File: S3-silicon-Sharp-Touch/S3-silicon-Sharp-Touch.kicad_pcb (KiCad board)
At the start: 4 copper layers, 79.8 x 44.7 mm, 64 parts, among them IC1 ESP32-S3FN8, J1 USB_C_Receptacle_USB2.0, J2 Conn_01x06_Socket, J3 Conn_01x11_Socket, J5 FH52-10S-0.5SH_99, J6 5024260810, J7 S2B-PH-SM4-TB_LF__SN_, Q1 MMBT3904, Q2 MMBT3904, Q3 Si2301CDS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

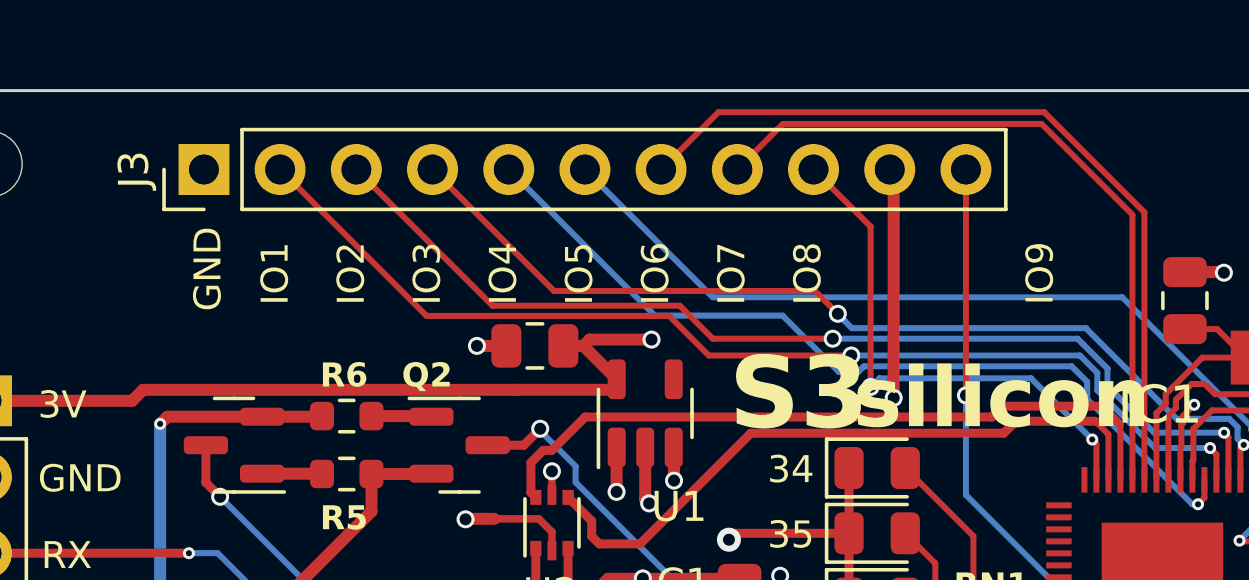
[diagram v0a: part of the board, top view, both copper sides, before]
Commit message: Update S3 silk
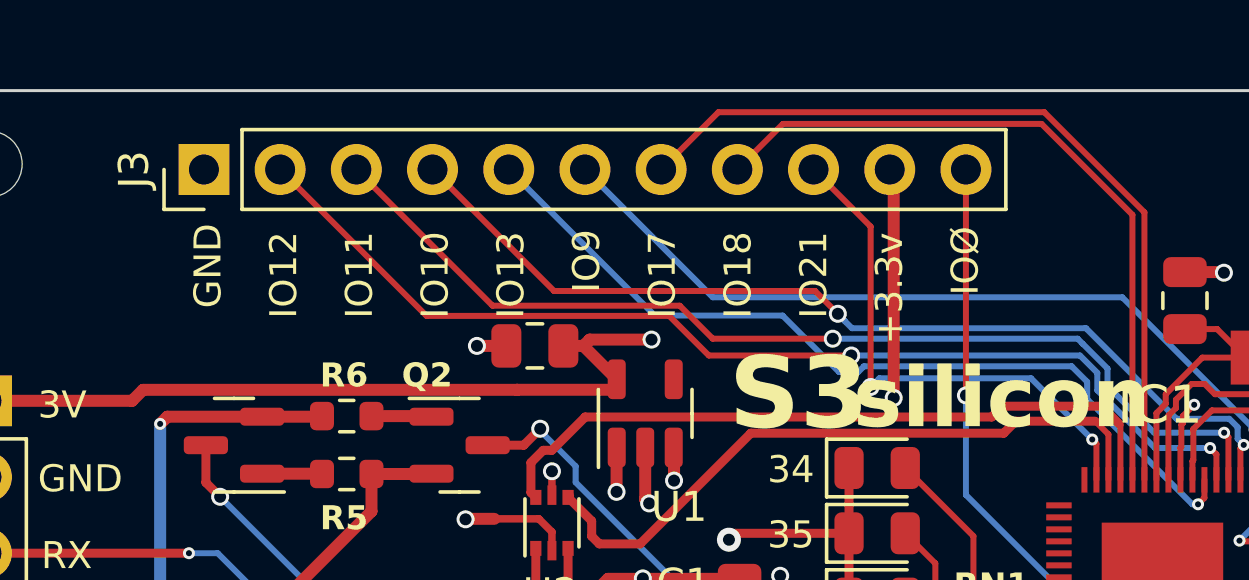
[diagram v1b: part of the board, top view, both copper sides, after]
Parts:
- added G***: LOGO, LOGO, B.Cu at (67.7, 59.6)
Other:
- board text added: "+3.3v"
- board text added: "IO10"
- board text added: "IO11"
- board text added: "IO12"
- board text added: "IO13"
- board text added: "IO17"
- board text added: "IO18"
- board text added: "IO21"
- board text added: "IOØ"
- board text added: "LCD IOs: IO - - - - - - 1 SPI_CLK 2 SPI_MOSI 3 CS 4 DISPON (pulled up) 14 EXTMODE"
- board text added: "TOUCH BITCH IO - - - - - 7 SCL (I2C) 8 SDA (I2C) 5 REST 6 IRQ (Interrupt)"
- board text removed: "IO1"
- board text removed: "IO2"
- board text removed: "IO3"
- board text removed: "IO4"
- board text removed: "IO5"
- board text removed: "IO6"
- board text removed: "IO7"
- board text removed: "IO8"

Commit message: 1.0 sent to fabrication
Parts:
- moved D7 3.80 mm to (59.7, 62.0), turned to -45 degrees
- moved D6 2.34 mm to (55.8, 61.9), turned to -135 degrees
- moved D1 0.94 mm to (59.8, 51.5), turned to 45 degrees
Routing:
- net VBUS: track 54.9 -> 60.3 mm
- net Net-(D6-K): track 2.14 -> 5.15 mm
- net Net-(D7-K): track 4.52 -> 6.96 mm
- net GND: track 58.7 -> 59.6 mm
- net VDD33: track 153.9 -> 154.5 mm
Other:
- board text added: "LCD pins: IO - - - - - - 1 SPI_CLK 2 SPI_MOSI 3 CS 4 DISPON (pulled up) 14 EXTMODE"
- board text added: "RDY"
- board text added: "TOUCH"
- board text added: "TOUCH BITCH IO - - - - - 7 SCL I2C 8 SDA I2C 5 REST 6 IRQ (Interrupt)"
- board text removed: "LCD IOs: IO - - - - - - 1 SPI_CLK 2 SPI_MOSI 3 CS 4 DISPON (pulled up) 14 EXTMODE"
- board text removed: "TOUCH BITCH IO - - - - - 7 SCL (I2C) 8 SDA (I2C) 5 REST 6 IRQ (Interrupt)"

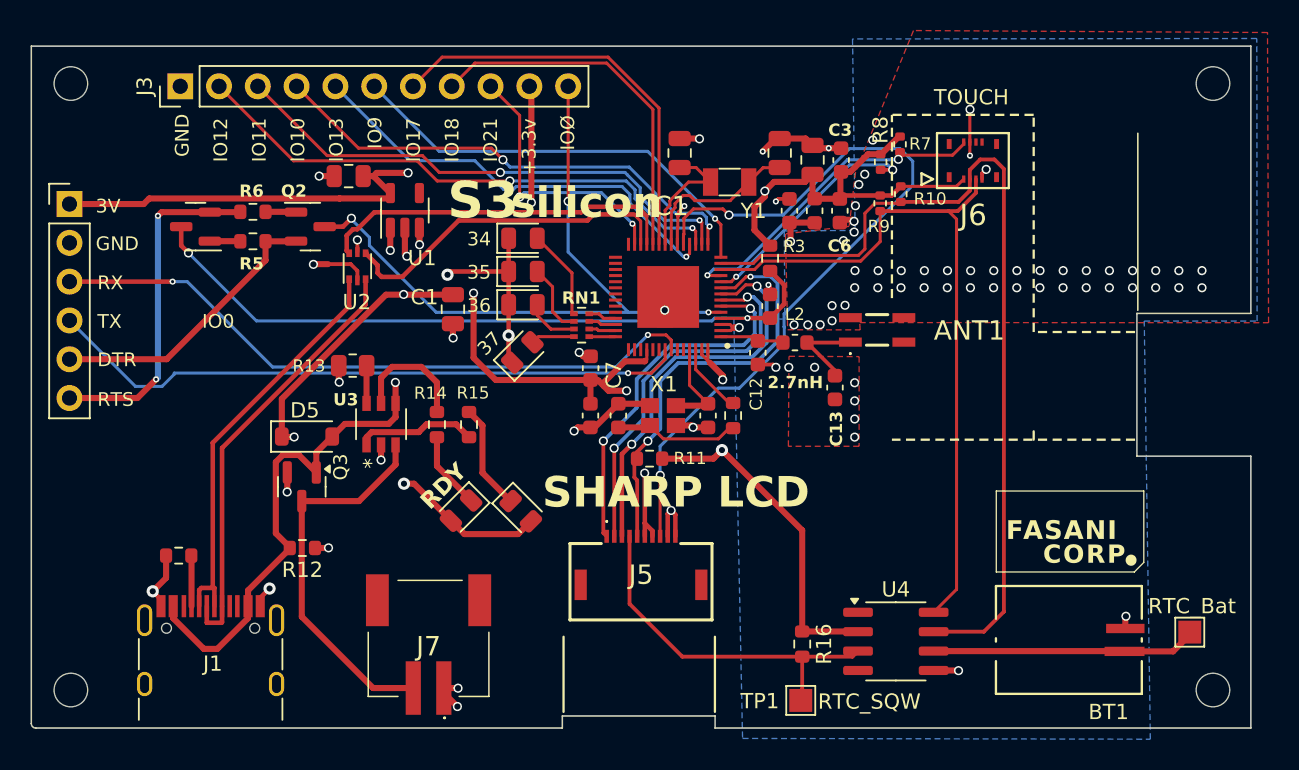
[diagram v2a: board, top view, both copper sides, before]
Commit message: Update BT1 routing because bad polarity
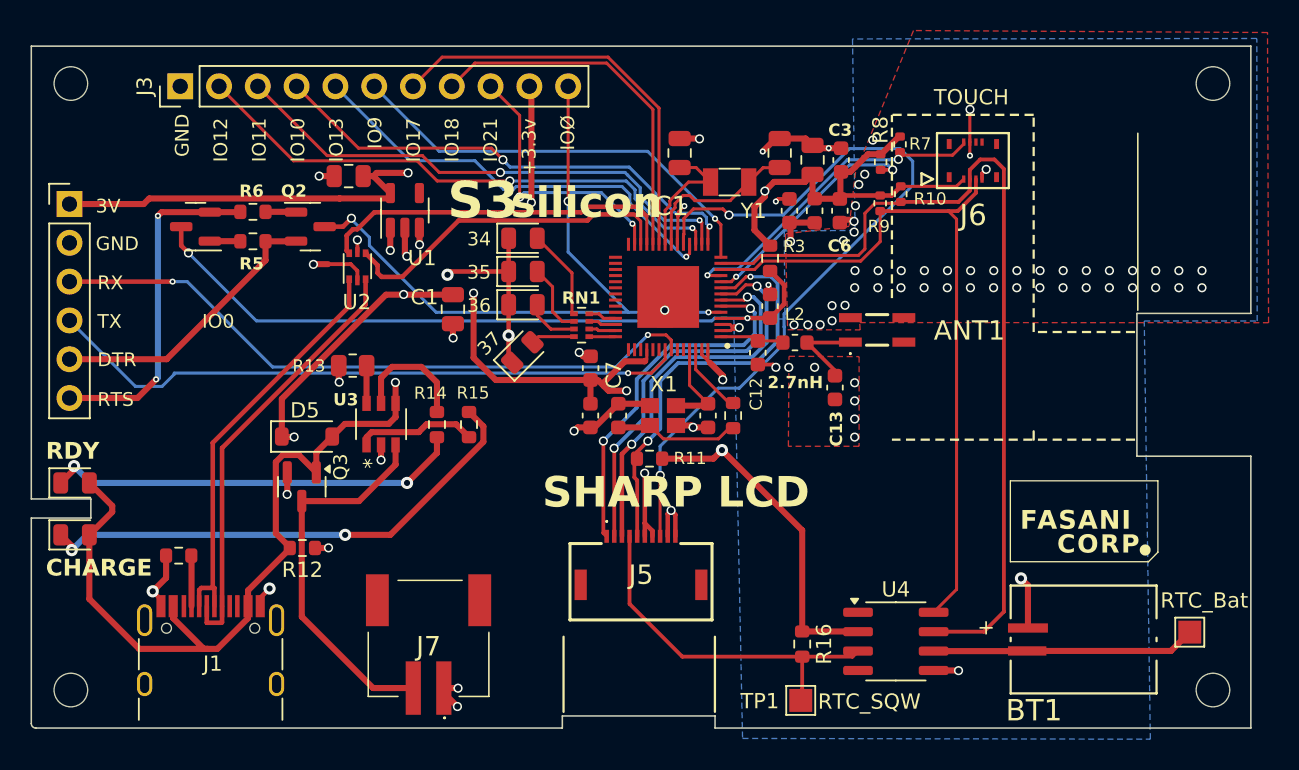
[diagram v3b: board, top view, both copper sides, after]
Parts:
- moved D7 29.2 mm to (30.5, 63.5), turned to 0 degrees
- moved D6 25.3 mm to (30.5, 60.1), turned to 0 degrees
- moved BT1 0.97 mm to (96.5, 70.3), turned to 0 degrees
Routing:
- net Net-(D7-K): track 6.96 -> 33.5 mm, vias 0 -> 2
- net Net-(D6-K): track 5.15 -> 27.5 mm, vias 0 -> 2
- net GND: track 59.6 -> 62.2 mm
- net VBUS: track 60.3 -> 61.3 mm, vias 3 -> 2
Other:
- outline, holes or cut-outs redrawn
- board text added: "CHARGE"

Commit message: Move touch 2 mm right
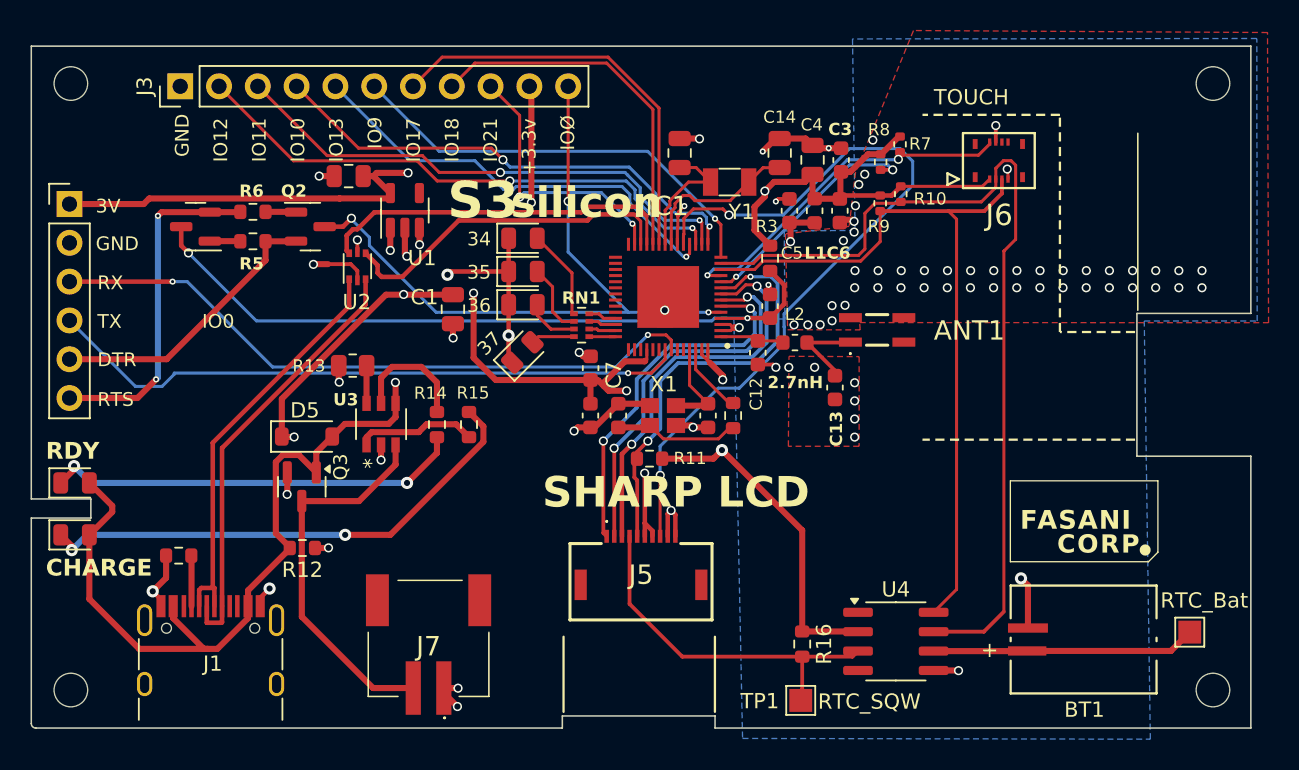
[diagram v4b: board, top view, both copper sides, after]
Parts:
- moved J6 1.70 mm to (91.0, 39.0)
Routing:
- net GND: track 62.2 -> 60.3 mm, vias 79 -> 78
- net /SCL: track 48.0 -> 49.7 mm
- net VDD33: track 154.5 -> 156.2 mm
- net /TOUCH_IRQ: track 21.8 -> 23.5 mm
- net /TOUCH_REST: track 22.2 -> 23.5 mm
- net /SDA: track 57.9 -> 59.0 mm

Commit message: Corrections heading to Rev 1.1 (Bottom ROW of Touch RIGHT!)
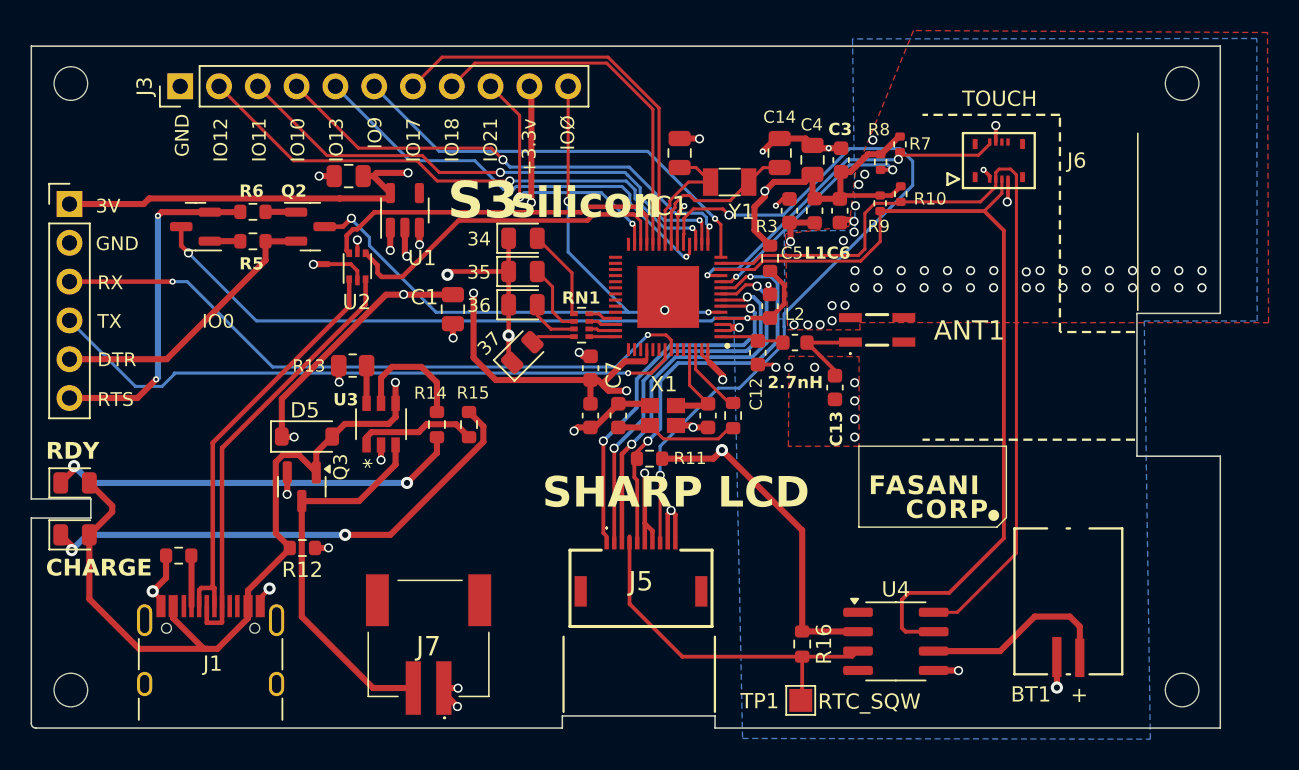
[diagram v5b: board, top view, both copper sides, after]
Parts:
- removed TP2: RTC_INT, TestPoint:TestPoint_Pad_1.5x1.5mm
- moved BT1 2.69 mm to (95.6, 67.9), turned to 90 degrees
- moved H2 2.02 mm to (103.0, 34.0)
- moved J5 0.43 mm to (67.6, 67.0)
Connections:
- IC1 pad 12: /SCL -> /SDA
- IC1 pad 13: /SDA -> /SCL
- R10 pad 2: /SDA -> /SCL
- R9 pad 2: /SCL -> /SDA
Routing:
- net VDD33: track 156.2 -> 167.8 mm, vias 8 -> 9
- net /SCL: track 49.7 -> 55.8 mm
- net VDD_RTC: track 17.3 -> 12.8 mm
- net /SDA: track 59.0 -> 56.9 mm
- net /TOUCH_REST: track 23.5 -> 22.1 mm
- net GND: track 60.3 -> 58.9 mm
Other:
- board size 79.8 x 44.7 mm -> 77.8 x 44.7 mm
- board text removed: "RTC_Bat"

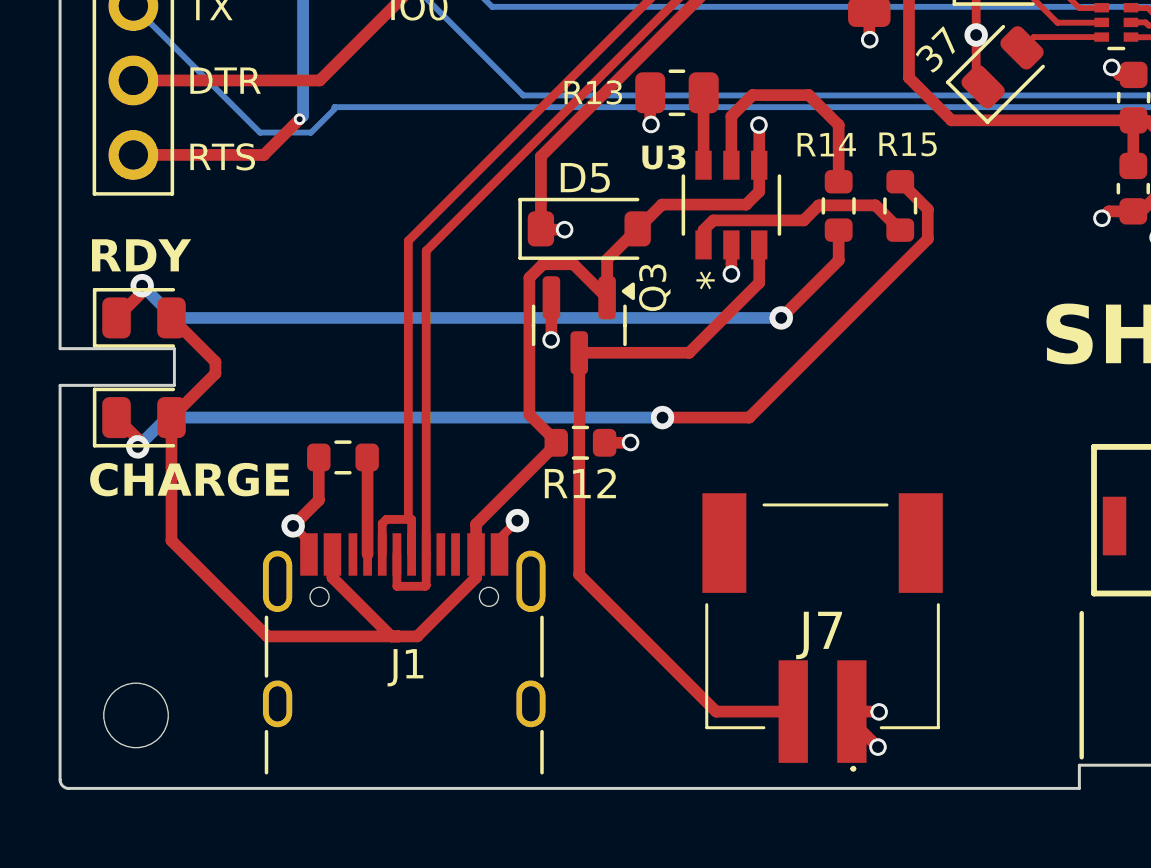
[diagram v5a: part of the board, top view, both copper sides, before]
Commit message: Update TOUCH pinout in PCBs
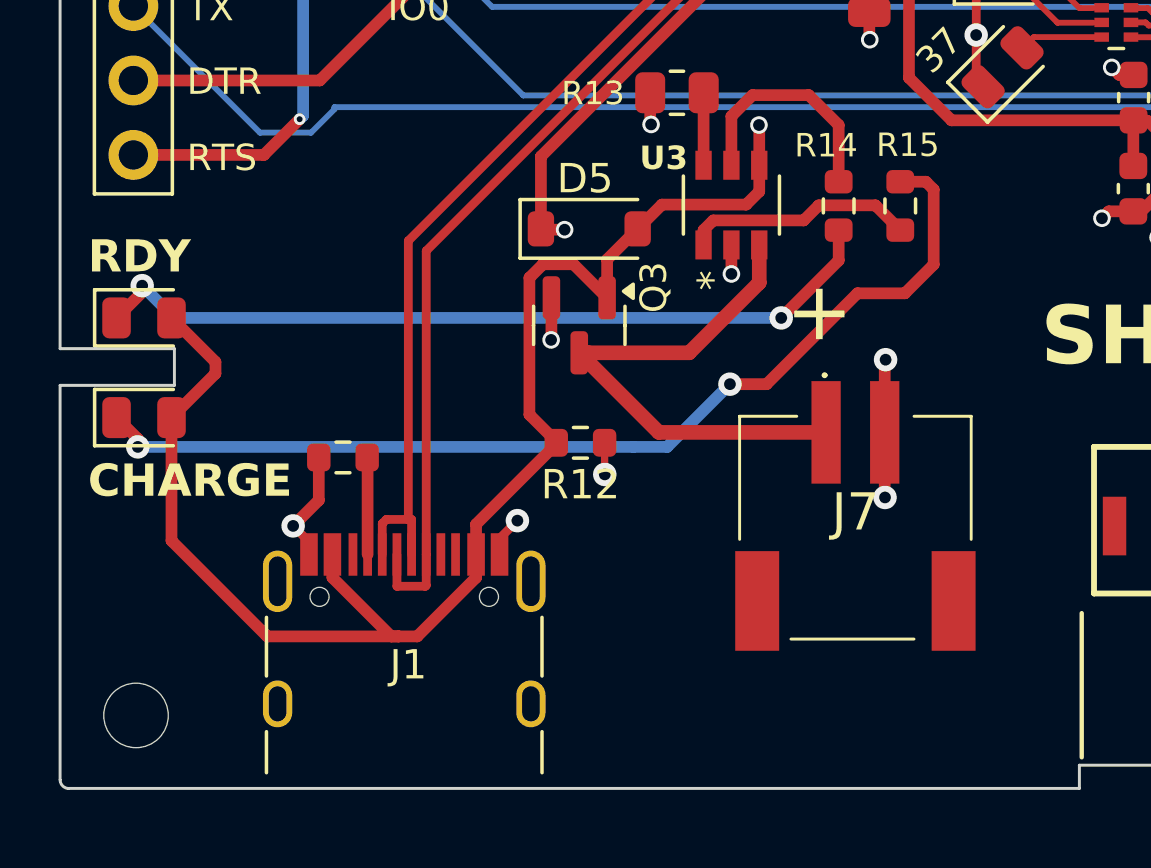
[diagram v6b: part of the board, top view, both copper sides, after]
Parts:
- moved J7 3.23 mm to (54.8, 67.3), turned to 180 degrees
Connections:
- J7 pad 1: GND -> VBAT
- J7 pad 2: VBAT -> GND
- R10 pad 2: /SCL -> /SDA
- R9 pad 2: /SDA -> /SCL
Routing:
- net VBAT: track 25.2 -> 18.0 mm
- net GND: track 58.9 -> 61.3 mm
- net Net-(D7-K): track 33.5 -> 34.8 mm
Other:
- board text added: "+"

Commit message: Heading for Rel 1.1
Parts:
- added J4: SM04B-SRSS-TB_LF__SN_, foot_sharp:QWIIC_SM04B-SRSS-TB_LFSN_, F.Cu at (71.7, 31.8)
- D1: value LED -> LED GREEN
- D4: value LED -> LED RED
- moved C15 1.55 mm to (68.8, 39.4), turned to 0 degrees
- moved R10 1.48 mm to (83.2, 41.8)
- moved R9 1.48 mm to (84.6, 41.2)
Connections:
- J7 pad 1: VBAT -> GND
- J7 pad 2: GND -> VBAT
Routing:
- net /SDA: track 56.9 -> 69.3 mm, vias 0 -> 2
- net /SCL: track 55.8 -> 66.9 mm, vias 0 -> 2
- net VDD33: track 167.8 -> 177.9 mm, vias 9 -> 10
- net VBAT: track 18.0 -> 24.1 mm
- net GND: track 61.3 -> 60.2 mm, vias 78 -> 77
- net /IO18: track 23.9 -> 22.9 mm
- net /IO17: track 27.2 -> 26.3 mm
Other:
- board text added: "QWIIC"
- board text added: "◀"

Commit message: S3 release 1.1 is ready
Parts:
- moved H4 2.02 mm to (103.0, 73.7)
- moved J6 0.50 mm to (91.5, 39.0)
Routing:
- net /SCL: track 66.9 -> 69.4 mm
- net /TOUCH_REST: track 22.1 -> 23.6 mm
- net /TOUCH_IRQ: track 23.5 -> 24.6 mm
